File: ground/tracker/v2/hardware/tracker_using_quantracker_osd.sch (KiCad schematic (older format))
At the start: 0 parts

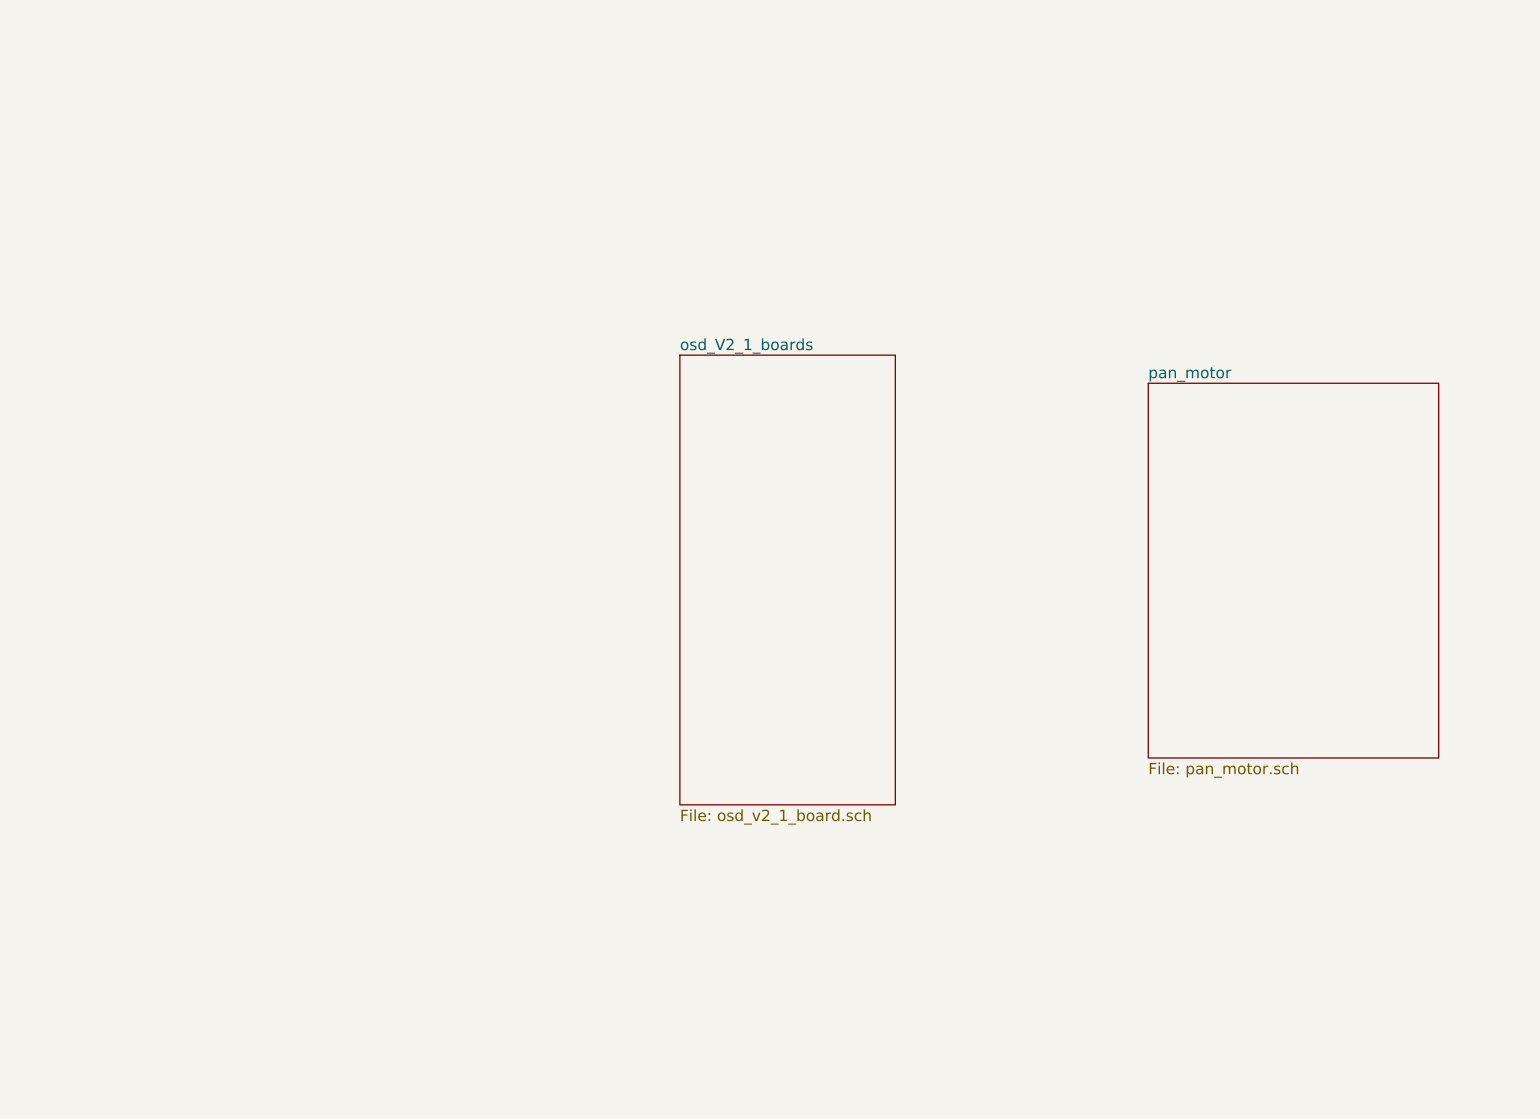
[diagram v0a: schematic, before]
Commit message: added FreeCAD design files for V2 tracker
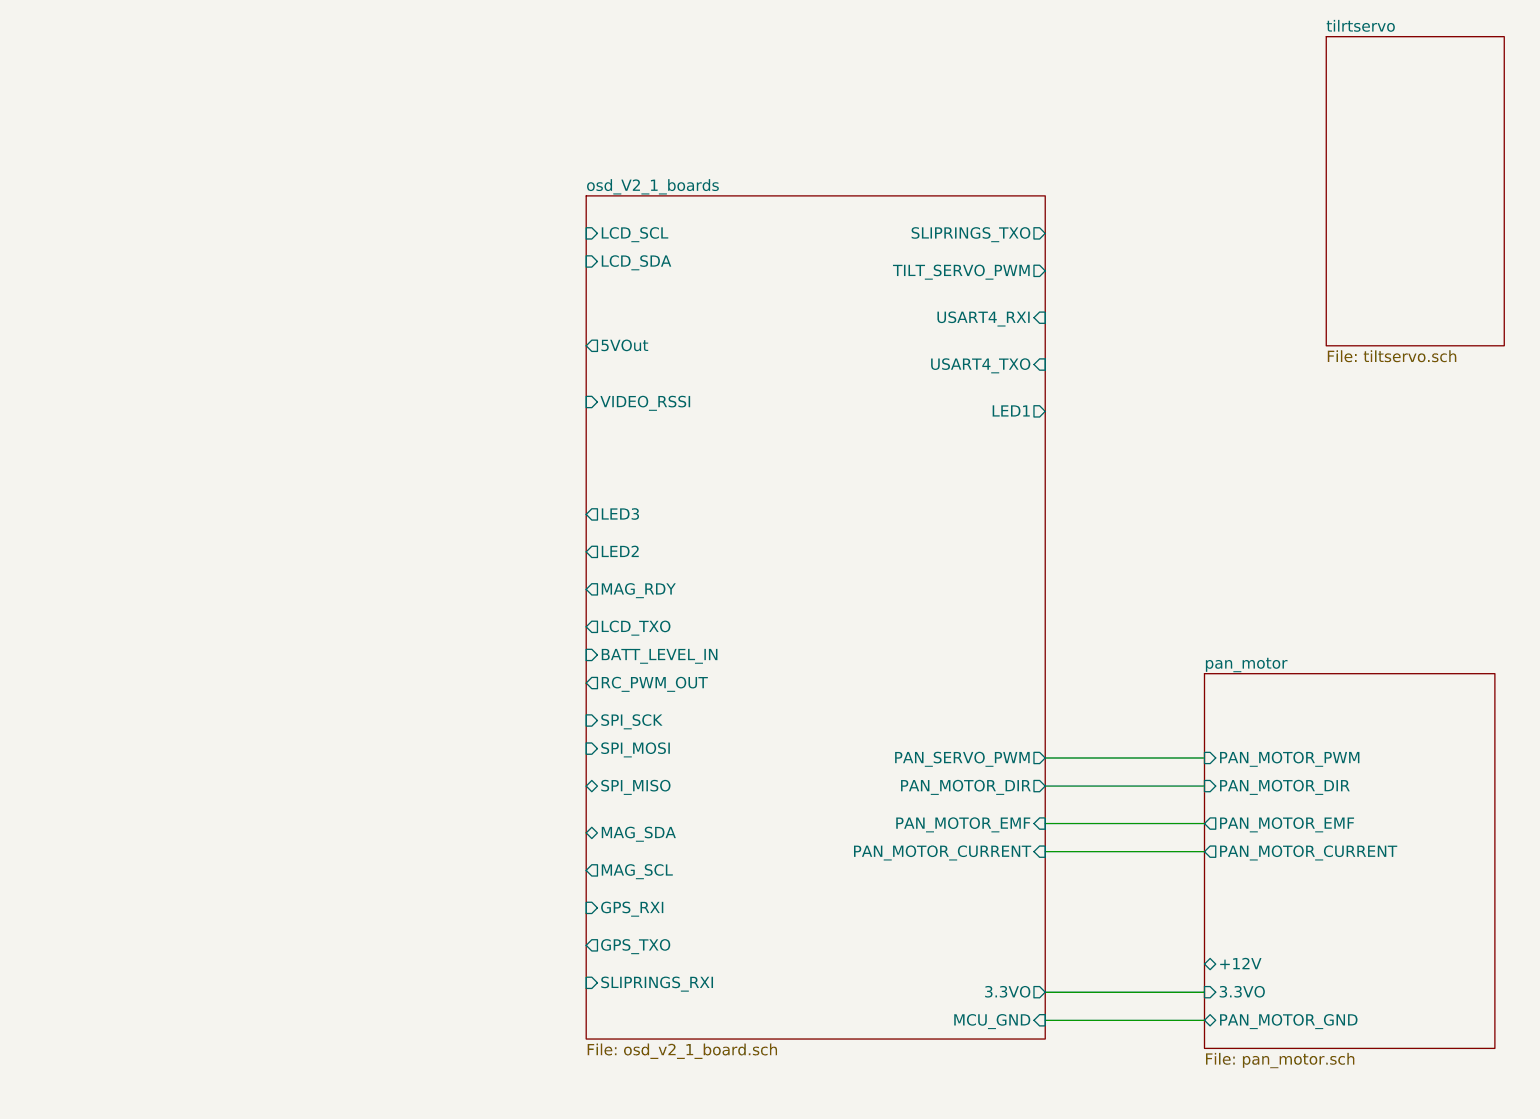
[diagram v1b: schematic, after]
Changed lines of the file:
@@
-EESchema Schematic File Version 2  date Fri 29 May 2015 09:32:36 BST
+EESchema Schematic File Version 2  date Mon 01 Jun 2015 18:53:27 BST
 LIBS:quantracker
 LIBS:stm32
@@
 LIBS:tcm3105
 LIBS:quantracker_air_osd_v2_1
+LIBS:mc34931
 LIBS:tracker_using_quantracker_osd-cache
 EELAYER 25  0
@@
 $Descr A4 11700 8267
 encoding utf-8
-Sheet 1 3
+Sheet 1 4
 Title ""
-Date "28 may 2015"
+Date "1 jun 2015"
 Rev ""
 Comp ""
@@
 Comment4 ""
 $EndDescr
+Wire Wire Line
+	7650 5950 6800 5950
+Wire Wire Line
+	6800 5200 7650 5200
+Wire Wire Line
+	6800 4850 7650 4850
+Wire Wire Line
+	6800 4700 7650 4700
+Wire Wire Line
+	6800 5050 7650 5050
+Wire Wire Line
+	6800 6100 7650 6100
 $Sheet
-S 7350 2700 1550 2000
+S 8300 850  950  1650
+U 556C873E
+F0 "tilrtservo" 60
+F1 "tiltservo.sch" 60
+$EndSheet
+$Sheet
+S 7650 4250 1550 2000
 U 555339C1
 F0 "pan_motor" 60
 F1 "pan_motor.sch" 60
+F2 "PAN_MOTOR_GND" B L 7650 6100 60
+F3 "PAN_MOTOR_CURRENT" O L 7650 5200 60
+F4 "3.3VO" I L 7650 5950 60
+F5 "+12V" B L 7650 5800 60
+F6 "PAN_MOTOR_PWM" I L 7650 4700 60
+F7 "PAN_MOTOR_DIR" I L 7650 4850 60
+F8 "PAN_MOTOR_EMF" O L 7650 5050 60
 $EndSheet
 $Sheet
-S 4850 2550 1150 2400
+S 4350 1700 2450 4500
 U 5551C6E9
 F0 "osd_V2_1_boards" 60
 F1 "osd_v2_1_board.sch" 60
+F2 "LCD_SCL" I L 4350 1900 60
+F3 "LCD_SDA" I L 4350 2050 60
+F4 "PAN_SERVO_PWM" O R 6800 4700 60
+F5 "5VOut" O L 4350 2500 60
+F6 "3.3VO" O R 6800 5950 60
+F7 "VIDEO_RSSI" I L 4350 2800 60
+F8 "PAN_MOTOR_CURRENT" I R 6800 5200 60
+F9 "PAN_MOTOR_EMF" I R 6800 5050 60
+F10 "LED3" O L 4350 3400 60
+F11 "LED2" O L 4350 3600 60
+F12 "MAG_RDY" O L 4350 3800 60
+F13 "LCD_TXO" O L 4350 4000 60
+F14 "BATT_LEVEL_IN" I L 4350 4150 60
+F15 "RC_PWM_OUT" O L 4350 4300 60
+F16 "SPI_SCK" I L 4350 4500 60
+F17 "SPI_MOSI" I L 4350 4650 60
+F18 "SPI_MISO" B L 4350 4850 60
+F19 "MAG_SDA" B L 4350 5100 60
+F20 "MAG_SCL" O L 4350 5300 60
+F21 "GPS_RXI" I L 4350 5500 60
+F22 "GPS_TXO" O L 4350 5700 60
+F23 "SLIPRINGS_RXI" I L 4350 5900 60
+F24 "SLIPRINGS_TXO" O R 6800 1900 60
+F25 "TILT_SERVO_PWM" O R 6800 2100 60
+F26 "USART4_RXI" I R 6800 2350 60
+F27 "USART4_TXO" I R 6800 2600 60
+F28 "LED1" O R 6800 2850 60
+F29 "PAN_MOTOR_DIR" O R 6800 4850 60
+F30 "MCU_GND" I R 6800 6100 60
 $EndSheet
 $EndSCHEMATC

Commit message: moved pin setup to libs, cleaned up osd_example1 makefie to use osd,osd.hpp, added some docs
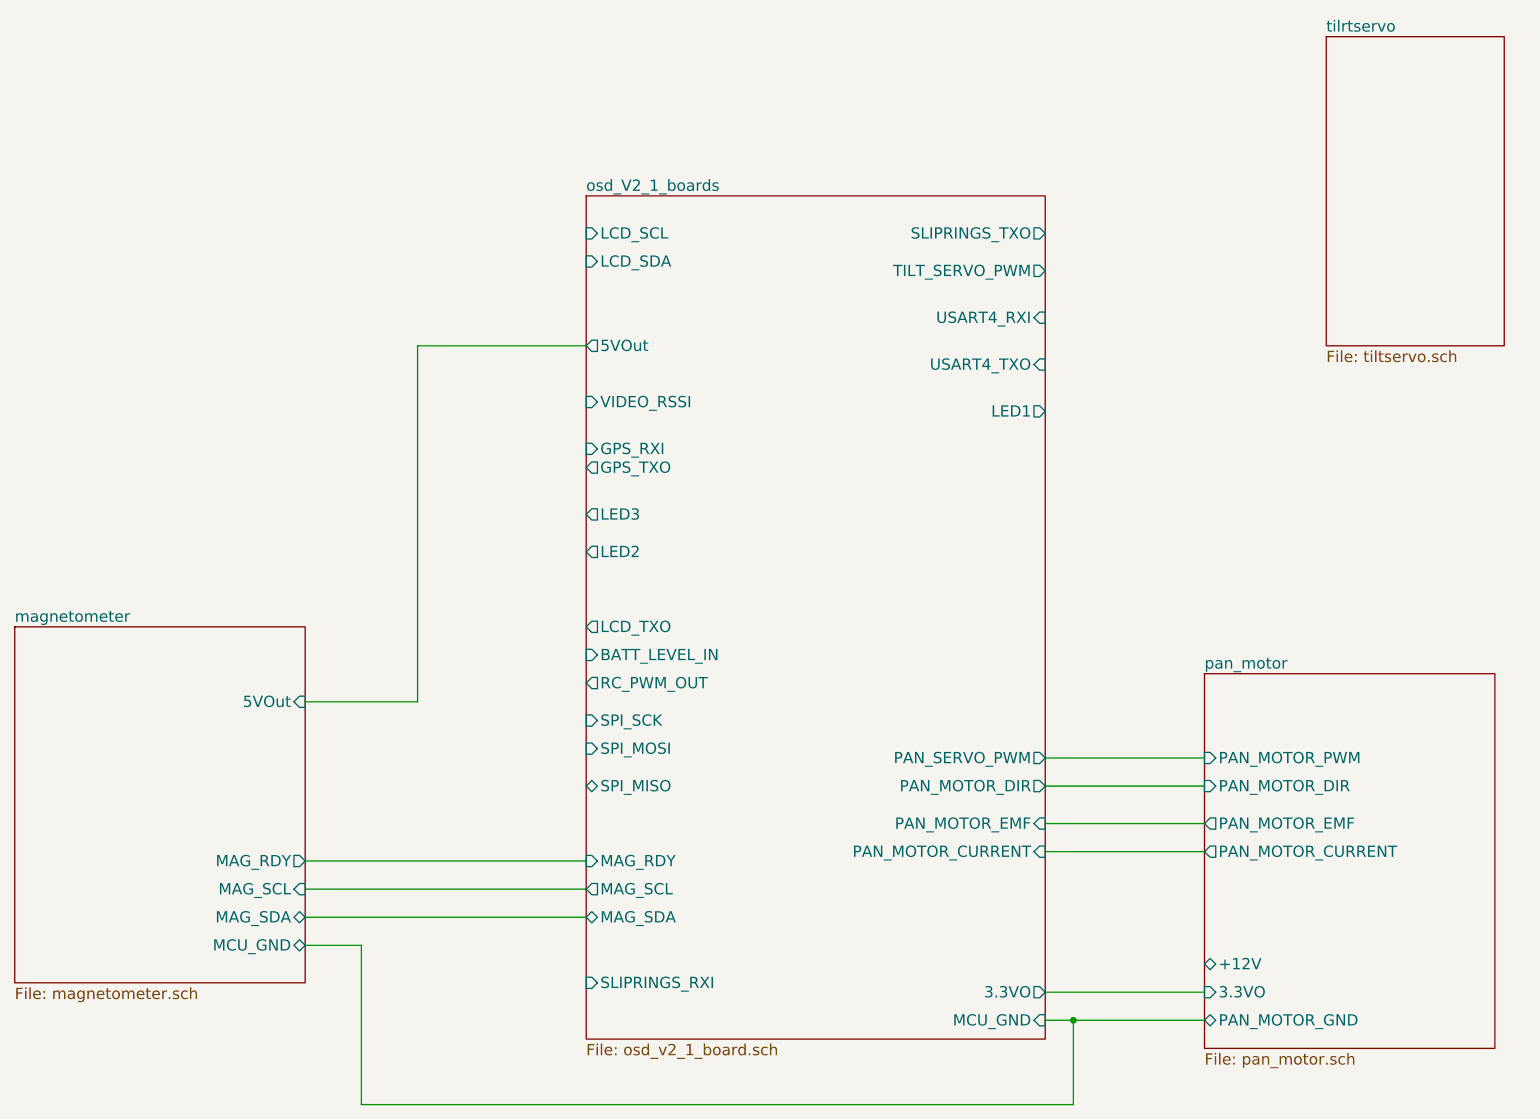
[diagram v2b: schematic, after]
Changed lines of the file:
@@
-EESchema Schematic File Version 2  date Mon 01 Jun 2015 18:53:27 BST
+EESchema Schematic File Version 2  date Sun 05 Jul 2015 19:04:22 BST
 LIBS:quantracker
 LIBS:stm32
@@
 $Descr A4 11700 8267
 encoding utf-8
-Sheet 1 4
+Sheet 1 5
 Title ""
-Date "1 jun 2015"
+Date "5 jul 2015"
 Rev ""
 Comp ""
@@
 $EndDescr
 Wire Wire Line
-	7650 5950 6800 5950
+	4350 5400 2850 5400
+Wire Wire Line
+	2850 5250 4350 5250
+Wire Wire Line
+	2850 5700 3150 5700
+Wire Wire Line
+	3150 5700 3150 6550
+Wire Wire Line
+	3150 6550 6950 6550
+Connection ~ 6950 6100
+Wire Wire Line
+	6950 6550 6950 6100
+Wire Wire Line
+	6800 6100 7650 6100
+Wire Wire Line
+	6800 5050 7650 5050
+Wire Wire Line
+	6800 4700 7650 4700
+Wire Wire Line
+	6800 4850 7650 4850
 Wire Wire Line
 	6800 5200 7650 5200
 Wire Wire Line
-	6800 4850 7650 4850
+	7650 5950 6800 5950
 Wire Wire Line
-	6800 4700 7650 4700
+	4350 2500 3450 2500
 Wire Wire Line
-	6800 5050 7650 5050
+	3450 2500 3450 4400
 Wire Wire Line
-	6800 6100 7650 6100
+	3450 4400 2850 4400
+Wire Wire Line
+	4350 5550 2850 5550
+$Sheet
+S 1300 4000 1550 1900
+U 55995FB3
+F0 "magnetometer" 60
+F1 "magnetometer.sch" 60
+F2 "MCU_GND" B R 2850 5700 60
+F3 "MAG_RDY" O R 2850 5250 60
+F4 "5VOut" I R 2850 4400 60
+F5 "MAG_SDA" B R 2850 5550 60
+F6 "MAG_SCL" I R 2850 5400 60
+$EndSheet
 $Sheet
 S 8300 850  950  1650
@@
 F10 "LED3" O L 4350 3400 60
 F11 "LED2" O L 4350 3600 60
-F12 "MAG_RDY" O L 4350 3800 60
+F12 "MAG_RDY" I L 4350 5250 60
 F13 "LCD_TXO" O L 4350 4000 60
 F14 "BATT_LEVEL_IN" I L 4350 4150 60
@@
 F17 "SPI_MOSI" I L 4350 4650 60
 F18 "SPI_MISO" B L 4350 4850 60
-F19 "MAG_SDA" B L 4350 5100 60
-F20 "MAG_SCL" O L 4350 5300 60
-F21 "GPS_RXI" I L 4350 5500 60
-F22 "GPS_TXO" O L 4350 5700 60
+F19 "MAG_SDA" B L 4350 5550 60
+F20 "MAG_SCL" O L 4350 5400 60
+F21 "GPS_RXI" I L 4350 3050 60
+F22 "GPS_TXO" O L 4350 3150 60
 F23 "SLIPRINGS_RXI" I L 4350 5900 60
 F24 "SLIPRINGS_TXO" O R 6800 1900 60

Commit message: tracker v2 commit bundle
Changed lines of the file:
@@
 $Descr A4 11693 8268
 encoding utf-8
-Sheet 1 5
+Sheet 1 6
 Title ""
 Date "10 dec 2015"
@@
 F30 "MCU_GND" I R 6800 6100 60
 $EndSheet
+$Sheet
+S 1750 1575 1150 925
+U 5B893130
+F0 "gps" 60
+F1 "gps.sch" 60
+$EndSheet
 $EndSCHEMATC
